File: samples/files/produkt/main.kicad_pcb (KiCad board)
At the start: 2 copper layers, 40.3 x 108.2 mm, 37 parts, among them J1 10 Pos, J2 01x05 Female, J3 01x03 Female, U1 TL072, U2 TL072, U3 AD633, U4 AD633, U5 TL072

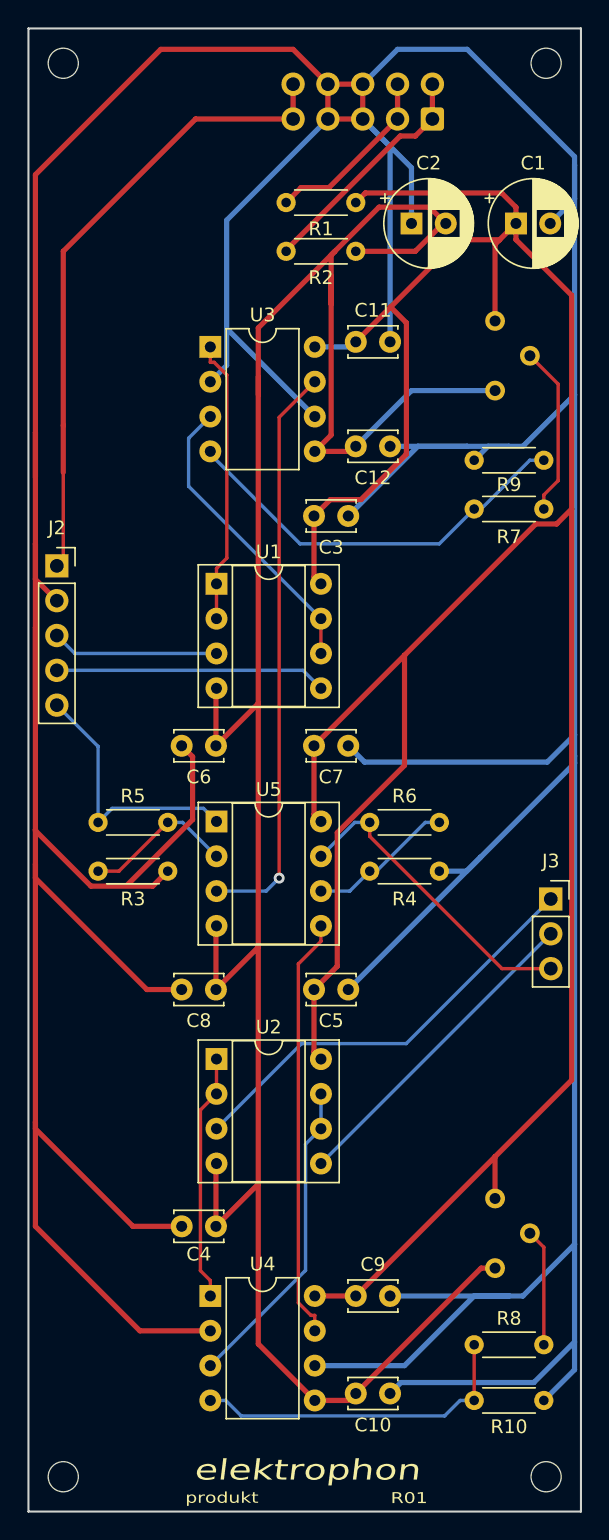
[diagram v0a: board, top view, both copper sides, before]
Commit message: parse kicad pcb files
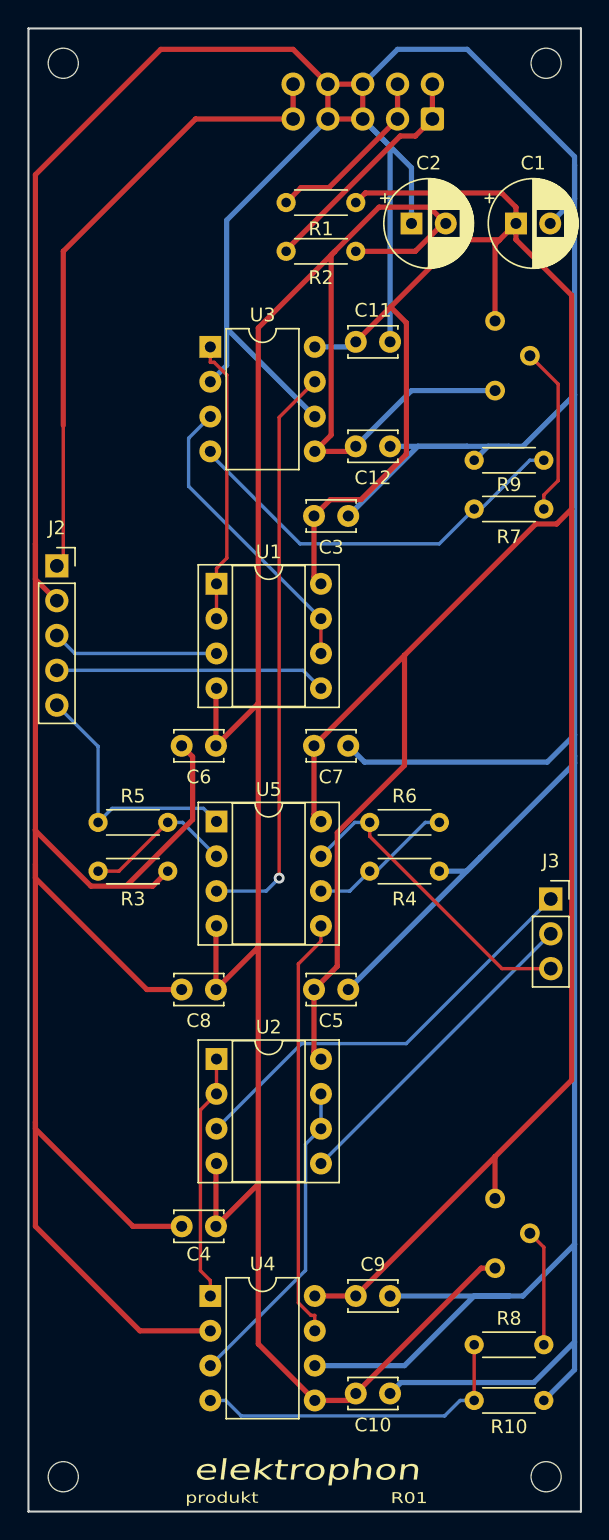
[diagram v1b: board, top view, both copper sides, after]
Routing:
- net GND: track 490.9 -> 481.8 mm
- net +5V: track 49.9 -> 46.4 mm
- net -15V: track 182.4 -> 179.1 mm
- net Net-(U2-Pad1): track 20.5 -> 18.1 mm
- net +15V: track 220.1 -> 219.6 mm
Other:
- net class Default removed
